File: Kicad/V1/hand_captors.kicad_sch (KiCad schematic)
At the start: 3 parts

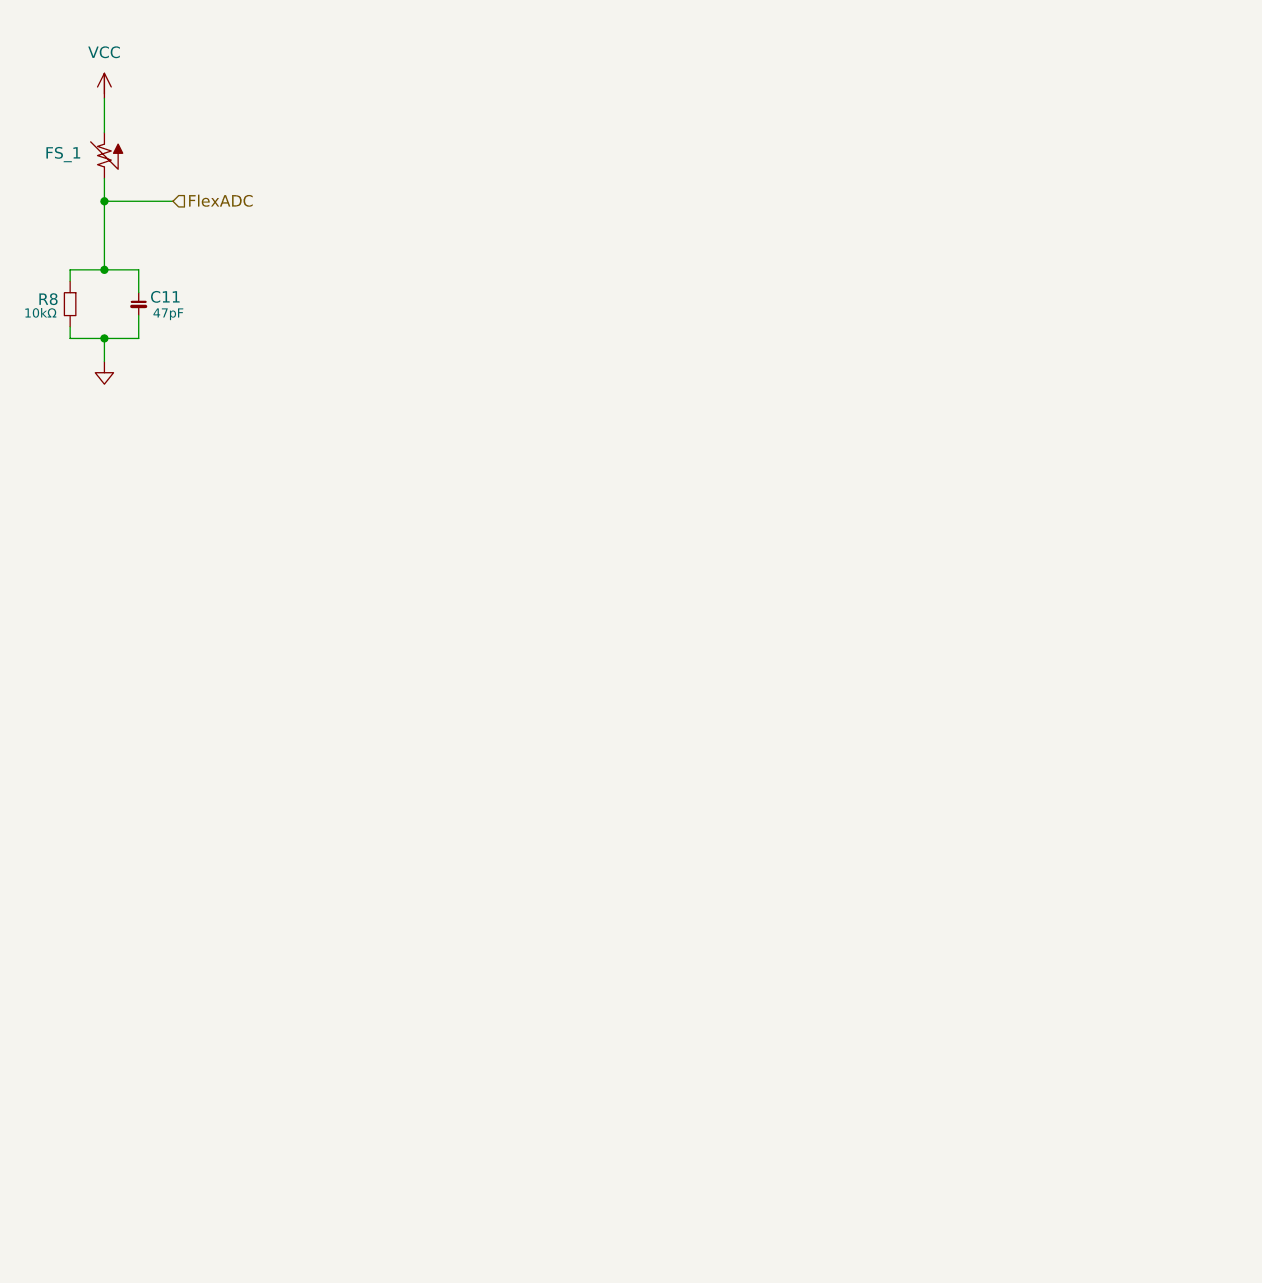
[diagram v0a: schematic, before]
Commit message: correction schema elec + ajout connecteur FPC
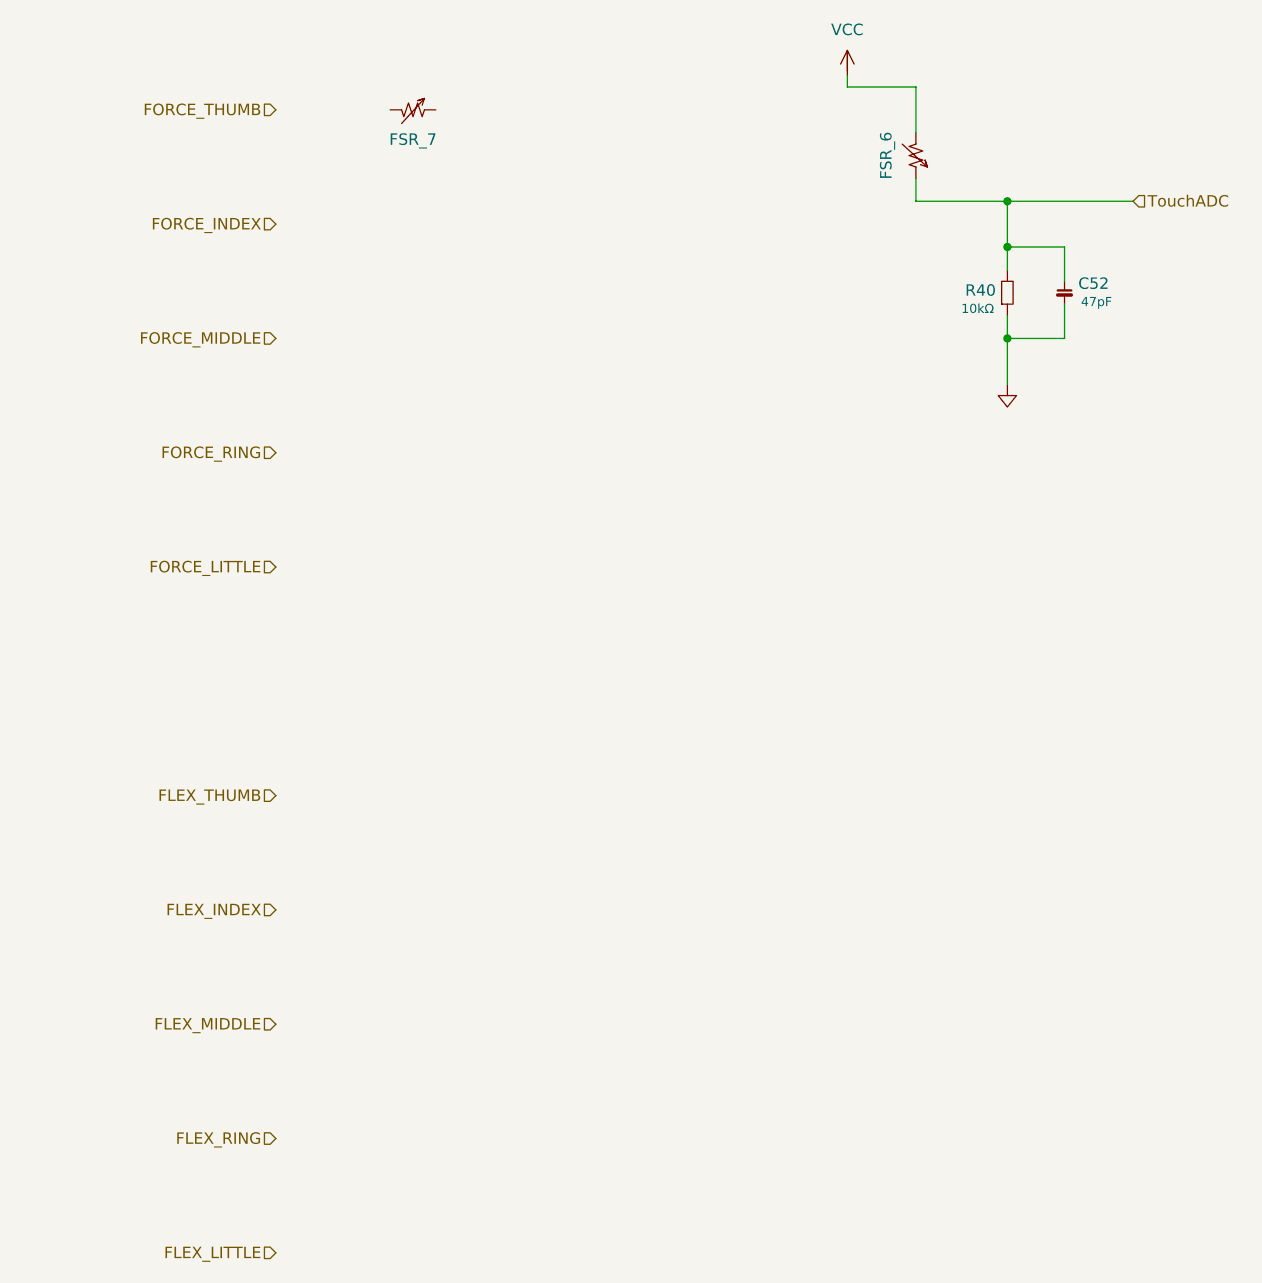
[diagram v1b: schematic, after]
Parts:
- removed C11: 47pF, MyGlove:Capacitor_0603, symbol G-Love:C
- removed FS_1: (no value), MyGlove:PinHeader_1x02_P2.54mm_Vertical, symbol G-Love:FS
- removed R8: 10kΩ, MyGlove:Resistor_0603, symbol G-Love:R
- added C52: 47pF, MyGlove:Capacitor_0603, symbol G-Love:C
- added FSR_6, FSR_7: (no value), MyGlove:PinHeader_1x02_P2.54mm_Vertical, symbol G-Love:FSR
- added R40: 10kΩ, MyGlove:Resistor_0603, symbol G-Love:R
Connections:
- net GND: now also C52.1, R40.1
- net VCC: now also FSR_6.2
- new net TouchADC: C52.2, FSR_6.1, R40.2
